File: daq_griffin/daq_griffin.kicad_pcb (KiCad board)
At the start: 4 copper layers, 80 x 117 mm, 203 parts, among them J1 SENSOR, J10 SENSOR, J11 SENSOR, J12 SENSOR, J13 SENSOR, J14 SENSOR, J15 SENSOR, J16 SENSOR, J17 SENSOR, J18 SENSOR, J19 SENSOR, J2 SENSOR, J20 SENSOR, J21 SENSOR, J22 SENSOR, J23 SENSOR, J24 SENSOR, J25 POWER_12V, J26 I2C Header, J27 CAN Header, J3 SENSOR, J4 SENSOR, J5 SENSOR, J6 SENSOR, J7 SENSOR, J8 SENSOR, J9 SENSOR, U13 ADS8866, U14 ADS8866, U15 ADS8866, U16 ADS8866, U17 ADS8866, U18 ADS8866, U19 ADS8866, U20 ADS8866, U21 ADS8866, U22 ADS8866, U23 ADS8866, U24 ADS8866, U25 TPS54302, U26 Teensy4.1, U29 REF6050xDGK, U30 TLV70933, U55 TCAN3414

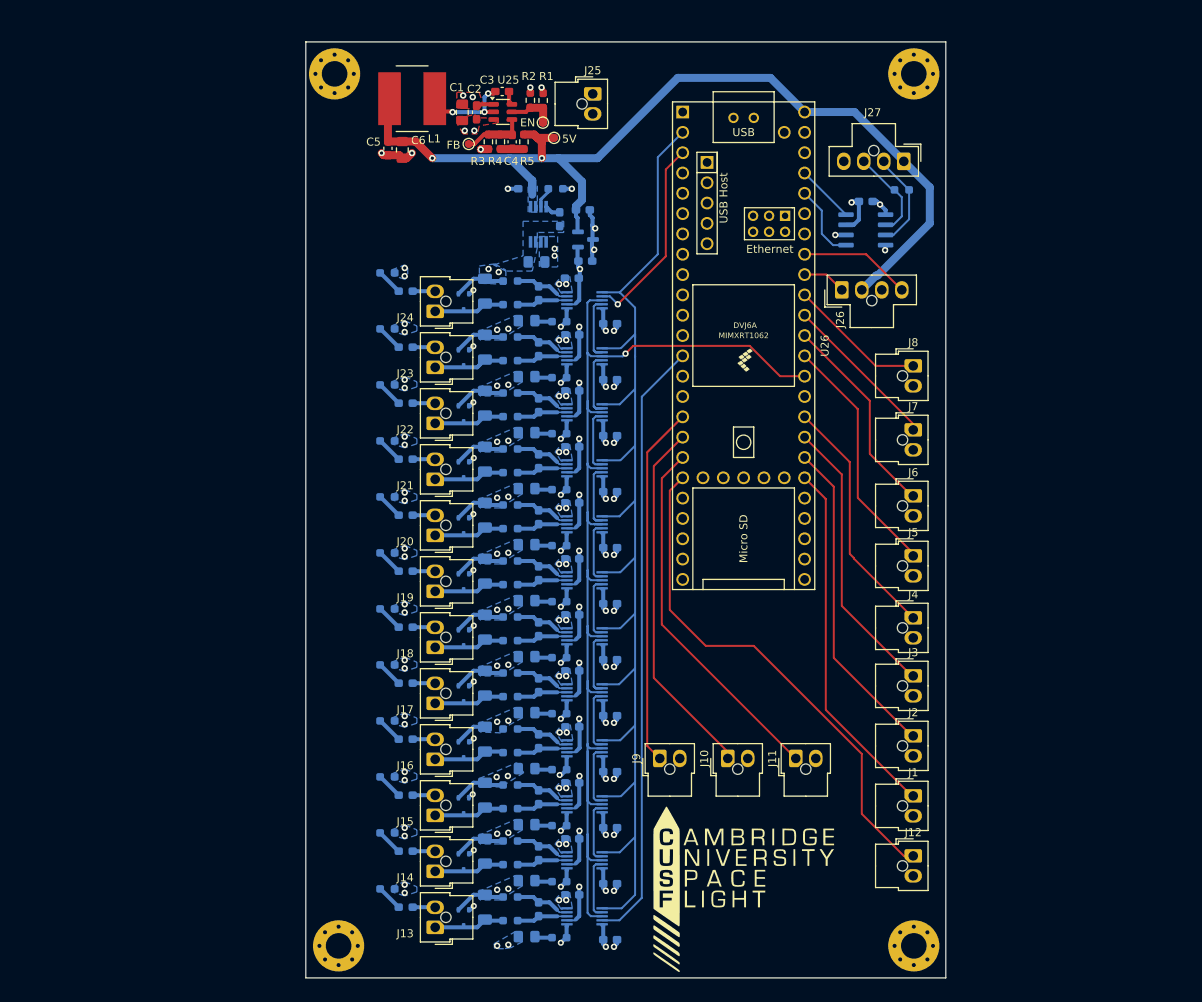
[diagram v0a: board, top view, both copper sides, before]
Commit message: Add 24V capability, add feed systems motor connections, fix SPI connections, add ignitor board connections, add i2c connections.
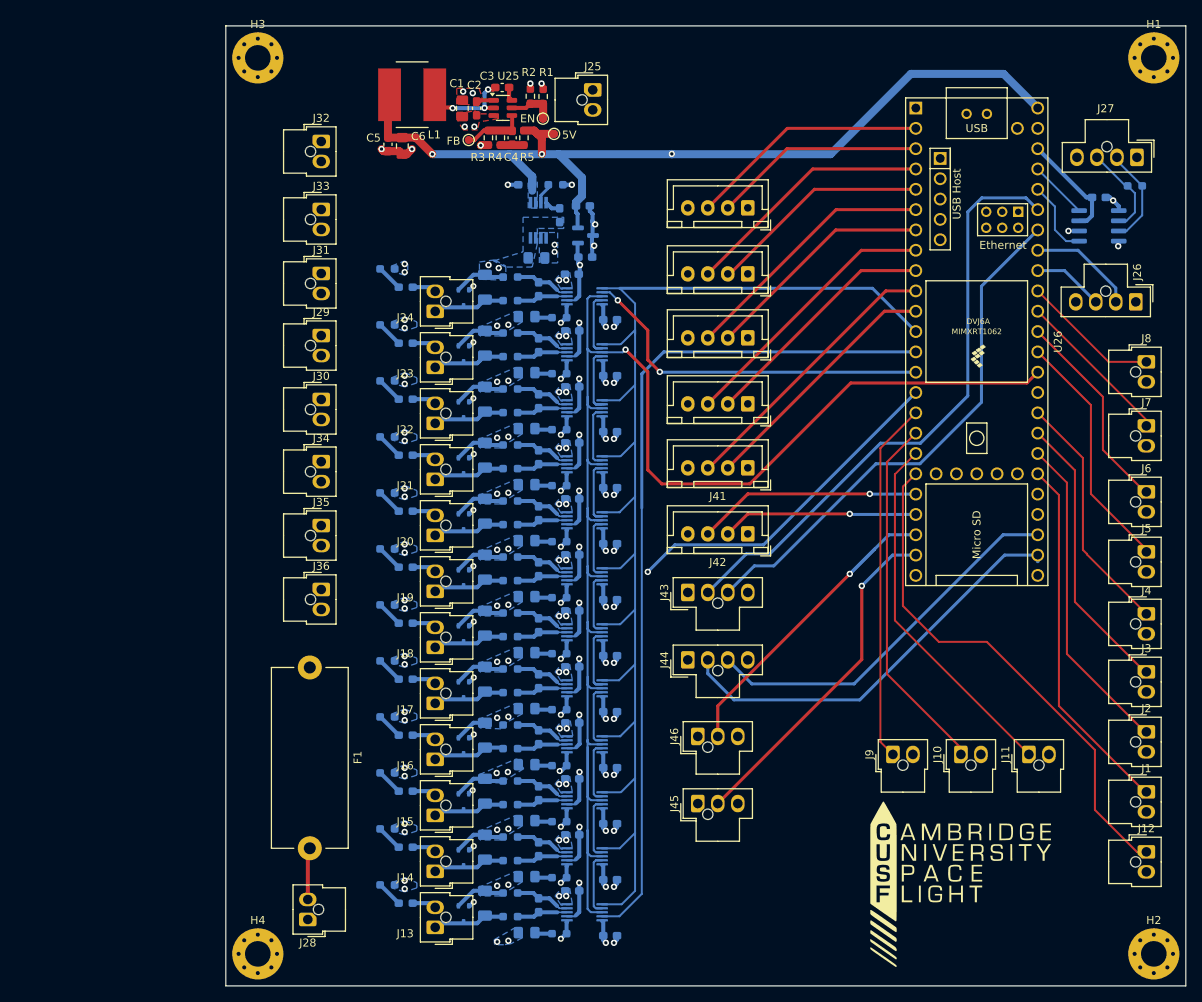
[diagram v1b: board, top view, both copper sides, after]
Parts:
- removed REF**, REF**1, REF**2, REF**3: MountingHole_3.2mm_M3_Pad_Via, MountingHole:MountingHole_3.2mm_M3_Pad_Via
- added F1: Fuse, Fuse:Fuseholder_Cylinder-5x20mm_Stelvio-Kontek_PTF78_Horizontal_Open, F.Cu at (90.5, 138.2)
- added H1: MountingHole_Pad, MountingHole:MountingHole_3.2mm_M3_Pad_Via, F.Cu at (196.0, 62.0)
- added H2: MountingHole_Pad, MountingHole:MountingHole_3.2mm_M3_Pad_Via, F.Cu at (196.0, 174.0)
- added H3: MountingHole_Pad, MountingHole:MountingHole_3.2mm_M3_Pad_Via, F.Cu at (84.0, 62.0)
- added H4: MountingHole_Pad, MountingHole:MountingHole_3.2mm_M3_Pad_Via, F.Cu at (84.0, 174.0)
- added J28: POWER_24V, Connector_Molex:Molex_Nano-Fit_105309-xx02_1x02_P2.50mm_Vertical, F.Cu at (90.2, 169.7)
- added J29: POWER_12V, Connector_Molex:Molex_Nano-Fit_105309-xx02_1x02_P2.50mm_Vertical, F.Cu at (91.9, 96.7)
- added J30: POWER_12V, Connector_Molex:Molex_Nano-Fit_105309-xx02_1x02_P2.50mm_Vertical, F.Cu at (91.9, 104.7)
- added J31: POWER_12V, Connector_Molex:Molex_Nano-Fit_105309-xx02_1x02_P2.50mm_Vertical, F.Cu at (91.9, 89.0)
- added J32: POWER_12V, Connector_Molex:Molex_Nano-Fit_105309-xx02_1x02_P2.50mm_Vertical, F.Cu at (91.9, 72.5)
- added J33: POWER_12V, Connector_Molex:Molex_Nano-Fit_105309-xx02_1x02_P2.50mm_Vertical, F.Cu at (91.9, 81.0)
- added J34: POWER_12V, Connector_Molex:Molex_Nano-Fit_105309-xx02_1x02_P2.50mm_Vertical, F.Cu at (91.9, 112.5)
- added J35: POWER_12V, Connector_Molex:Molex_Nano-Fit_105309-xx02_1x02_P2.50mm_Vertical, F.Cu at (91.9, 120.5)
- added J36: POWER_12V, Connector_Molex:Molex_Nano-Fit_105309-xx02_1x02_P2.50mm_Vertical, F.Cu at (91.9, 128.4)
- added J37: Conn_01x04_Socket, Connector_JST:JST_XH_B4B-XH-A_1x04_P2.50mm_Vertical, F.Cu at (145.2, 89.0)
- added J38: Conn_01x04_Socket, Connector_JST:JST_XH_B4B-XH-A_1x04_P2.50mm_Vertical, F.Cu at (145.2, 80.8)
- added J39: Conn_01x04_Socket, Connector_JST:JST_XH_B4B-XH-A_1x04_P2.50mm_Vertical, F.Cu at (145.2, 97.0)
- added J40: Conn_01x04_Socket, Connector_JST:JST_XH_B4B-XH-A_1x04_P2.50mm_Vertical, F.Cu at (145.2, 105.2)
- added J41: Conn_01x04_Socket, Connector_JST:JST_XH_B4B-XH-A_1x04_P2.50mm_Vertical, F.Cu at (145.2, 113.2)
- added J42: Conn_01x04_Socket, Connector_JST:JST_XH_B4B-XH-A_1x04_P2.50mm_Vertical, F.Cu at (145.2, 121.5)
- added J43: UART Header, Connector_Molex:Molex_Nano-Fit_105309-xx04_1x04_P2.50mm_Vertical, F.Cu at (137.8, 128.8)
- added J44: UART Header, Connector_Molex:Molex_Nano-Fit_105309-xx04_1x04_P2.50mm_Vertical, F.Cu at (137.8, 137.2)
- added J45: Conn_01x03_Socket, Connector_Molex:Molex_Nano-Fit_105309-xx03_1x03_P2.50mm_Vertical, F.Cu at (139.0, 155.2)
- added J46: Conn_01x03_Socket, Connector_Molex:Molex_Nano-Fit_105309-xx03_1x03_P2.50mm_Vertical, F.Cu at (139.0, 146.8)
- moved J26 36.8 mm to (193.8, 92.5), turned to -90 degrees
- moved U26 29.1 mm to (173.9, 97.5)
- moved C113 29.1 mm to (189.1, 79.4)
- moved J1 29.1 mm to (195.1, 153.8)
- moved J10 29.1 mm to (171.9, 149.1)
- moved J11 29.1 mm to (180.4, 149.1)
- moved J12 29.1 mm to (195.1, 161.2)
- moved J2 29.1 mm to (195.1, 146.2)
- moved J27 29.1 mm to (193.9, 74.4)
- moved J3 29.1 mm to (195.1, 138.8)
- moved J4 29.1 mm to (195.1, 131.5)
- moved J5 29.1 mm to (195.1, 123.8)
- moved J6 29.1 mm to (195.1, 116.2)
- moved J7 29.1 mm to (195.1, 108.0)
- moved J8 29.1 mm to (195.1, 100.0)
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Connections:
- net /MOSI2 renamed /ADC_Chain2/MOSI
- C113 pad 1: +3.3V -> Net-(U55-VCC)
- J11 pad 1: Net-(J11-Pin_1) -> GND
- J26 pad 1: Net-(J26-Pin_1) -> GND
- J26 pad 2: +5V -> Net-(J26-Pin_2)
- J26 pad 3: GND -> Net-(J26-Pin_3)
- J26 pad 4: Net-(J26-Pin_4) -> +5V
- J27 pad 1: +5V -> GND
- J27 pad 4: GND -> +5V
- U26 pad 10: unconnected-(U26-8_TX2_IN1-Pad10) -> Net-(J41-Pin_3)
- U26 pad 11: unconnected-(U26-9_OUT1C-Pad11) -> Net-(J41-Pin_2)
- U26 pad 12: unconnected-(U26-10_CS_MQSR-Pad12) -> /ADC_Chain2/CS
- U26 pad 14: unconnected-(U26-12_MISO_MQSL-Pad14) -> /ADC_Chain2/MISO
- U26 pad 15: unconnected-(U26-3V3-Pad15) -> +3.3V
- U26 pad 18: Net-(J11-Pin_1) -> GND
- U26 pad 2: /ADC_Chain2/CS -> Net-(J38-Pin_3)
- U26 pad 20: unconnected-(U26-28_RX7-Pad20) -> Net-(J42-Pin_3)
- U26 pad 21: unconnected-(U26-29_TX7-Pad21) -> Net-(J42-Pin_2)
- U26 pad 22: unconnected-(U26-30_CRX3-Pad22) -> Net-(J46-Pin_2)
- U26 pad 23: unconnected-(U26-31_CTX3-Pad23) -> Net-(J45-Pin_2)
- U26 pad 26: unconnected-(U26-34_RX8-Pad26) -> Net-(J44-Pin_2)
- U26 pad 27: unconnected-(U26-35_TX8-Pad27) -> Net-(J44-Pin_3)
- U26 pad 3: /ADC_Chain2/MISO -> Net-(J38-Pin_2)
- U26 pad 4: unconnected-(U26-2_OUT2-Pad4) -> Net-(J37-Pin_3)
- U26 pad 40: Net-(J26-Pin_1) -> Net-(J26-Pin_3)
- U26 pad 41: Net-(J26-Pin_4) -> Net-(J26-Pin_2)
- U26 pad 42: unconnected-(U26-20_A6_TX5_LRCLK1-Pad42) -> Net-(J43-Pin_3)
- U26 pad 43: unconnected-(U26-21_A7_RX5_BCLK1-Pad43) -> Net-(J43-Pin_2)
- U26 pad 46: +3.3V -> Net-(U55-VCC)
- U26 pad 5: unconnected-(U26-3_LRCLK2-Pad5) -> Net-(J37-Pin_2)
- U26 pad 6: unconnected-(U26-4_BCLK2-Pad6) -> Net-(J39-Pin_3)
- U26 pad 7: unconnected-(U26-5_IN2-Pad7) -> Net-(J39-Pin_2)
- U26 pad 8: unconnected-(U26-6_OUT1D-Pad8) -> Net-(J40-Pin_3)
- U26 pad 9: unconnected-(U26-7_RX2_OUT1A-Pad9) -> Net-(J40-Pin_2)
- U55 pad 3: +3.3V -> Net-(U55-VCC)
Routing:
- net Net-(J43-Pin_2): track 0.00 -> 75.8 mm
- net Net-(J43-Pin_3): track 0.00 -> 66.0 mm
- net Net-(J44-Pin_2): track 0.00 -> 52.6 mm
- net Net-(J44-Pin_3): track 0.00 -> 47.7 mm
- net /SCLK2: track 142.7 -> 189.8 mm
- net GND: track 108.4 -> 154.1 mm
- net Net-(J11-Pin_1): track 45.6 -> 0.00 mm
- net Net-(J45-Pin_2): track 0.00 -> 43.0 mm, vias 0 -> 1
- net Net-(J46-Pin_2): track 0.00 -> 41.8 mm, vias 0 -> 1
- net +3.3V: track 40.7 -> 78.3 mm
- net Net-(J41-Pin_3): track 0.00 -> 35.2 mm
- net Net-(J40-Pin_3): track 0.00 -> 34.0 mm
- net Net-(J39-Pin_3): track 0.00 -> 32.6 mm
- net Net-(J41-Pin_2): track 0.00 -> 31.6 mm
- net Net-(J37-Pin_3): track 0.00 -> 31.4 mm
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- added copper zone on In1.Cu, net +24V
- added copper zone on In1.Cu, net +5V
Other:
- board size 80 x 117 mm -> 120 x 120 mm

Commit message: Rewired right side and fixed dual transistor
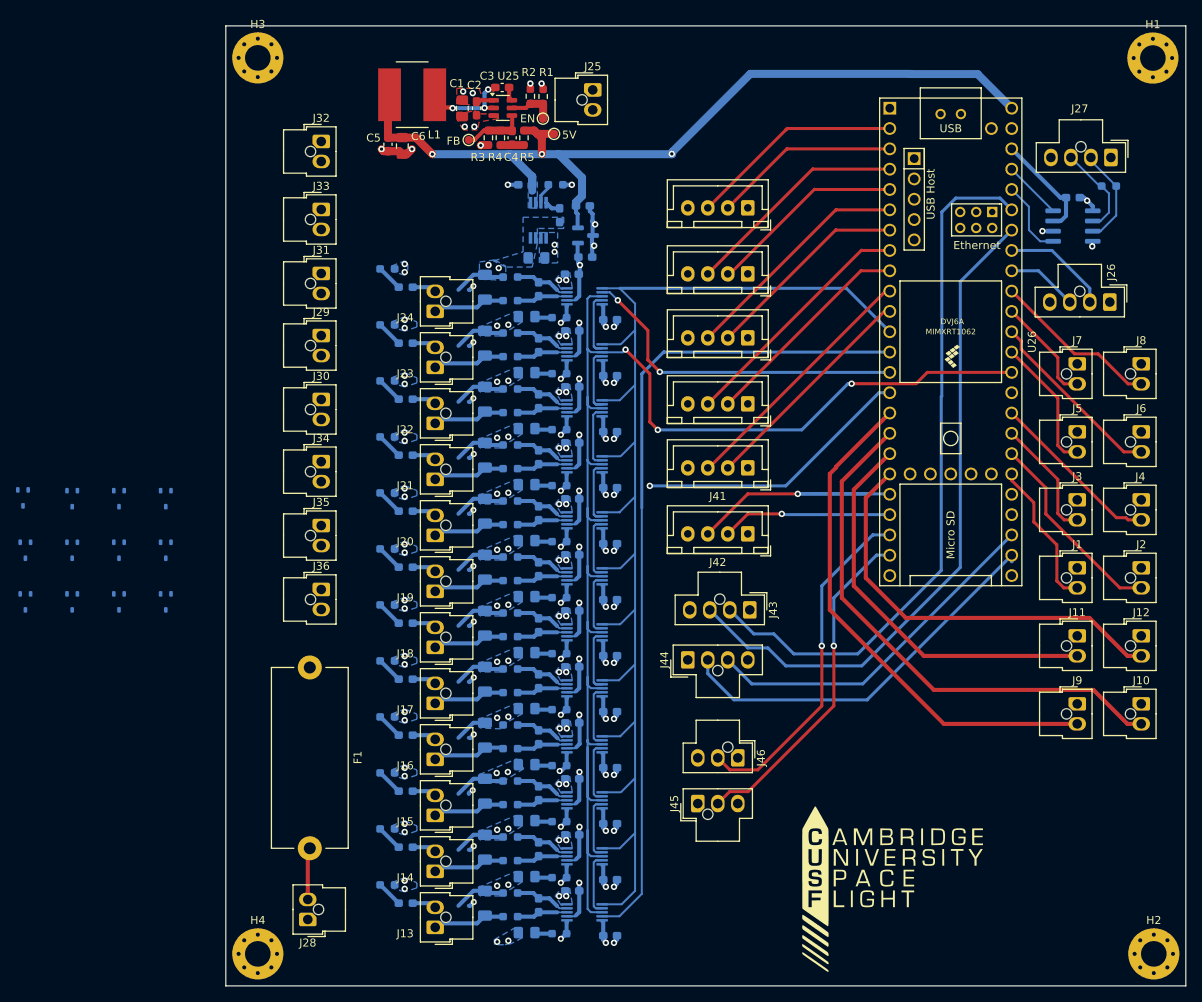
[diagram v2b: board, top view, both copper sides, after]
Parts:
- removed D13, D14, D15, D16, D17, D18, D19, D20, D21, D22, D23, D24: BAT54SW, Package_TO_SOT_SMD:SOT-323_SC-70
- added D1: BAV99, Package_TO_SOT_SMD:SOT-323_SC-70, B.Cu at (54.6, 117.0)
- added D10: BAV99, Package_TO_SOT_SMD:SOT-323_SC-70, B.Cu at (72.5, 130.0)
- added D11: BAV99, Package_TO_SOT_SMD:SOT-323_SC-70, B.Cu at (72.5, 117.1)
- added D12: BAV99, Package_TO_SOT_SMD:SOT-323_SC-70, B.Cu at (66.7, 117.1)
- added D2: BAV99, Package_TO_SOT_SMD:SOT-323_SC-70, B.Cu at (55.0, 130.0)
- added D3: BAV99, Package_TO_SOT_SMD:SOT-323_SC-70, B.Cu at (60.8, 130.0)
- added D4: BAV99, Package_TO_SOT_SMD:SOT-323_SC-70, B.Cu at (55.0, 123.5)
- added D5: BAV99, Package_TO_SOT_SMD:SOT-323_SC-70, B.Cu at (66.7, 123.5)
- added D6: BAV99, Package_TO_SOT_SMD:SOT-323_SC-70, B.Cu at (60.8, 117.1)
- added D7: BAV99, Package_TO_SOT_SMD:SOT-323_SC-70, B.Cu at (60.8, 123.5)
- added D8: BAV99, Package_TO_SOT_SMD:SOT-323_SC-70, B.Cu at (66.7, 130.0)
- added D9: BAV99, Package_TO_SOT_SMD:SOT-323_SC-70, B.Cu at (72.5, 123.5)
- J29, J30, J31, J32, J33, J34, J35, J36: value POWER_12V -> POWER_24V
- moved J1 29.3 mm to (186.4, 125.8)
- moved J12 27.0 mm to (194.4, 134.2)
- moved J9 23.9 mm to (186.4, 142.8), turned to 0 degrees
- moved J10 23.4 mm to (194.4, 142.8), turned to 0 degrees
- moved J3 23.2 mm to (186.4, 117.2)
- moved J2 20.5 mm to (194.4, 125.8)
- moved J5 17.3 mm to (186.4, 108.8)
- moved J11 16.0 mm to (186.4, 134.2), turned to 0 degrees
- moved J4 14.3 mm to (194.4, 117.2)
- moved J7 11.6 mm to (186.4, 100.2)
- moved J43 8.05 mm to (145.5, 131.0), turned to -90 degrees
- moved J6 7.53 mm to (194.4, 108.8)
- moved J46 5.67 mm to (144.0, 149.5), turned to -90 degrees
- moved C113 3.25 mm to (185.9, 79.5)
- moved J26 3.25 mm to (190.5, 92.5)
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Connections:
- J1 pad 1: Net-(J1-Pin_1) -> GND
- J1 pad 2: GND -> Net-(J1-Pin_2)
- J10 pad 1: Net-(J10-Pin_1) -> GND
- J10 pad 2: GND -> Net-(J10-Pin_2)
- J11 pad 2: GND -> Net-(J11-Pin_2)
- J12 pad 1: Net-(J12-Pin_1) -> GND
- J12 pad 2: GND -> Net-(J12-Pin_2)
- J2 pad 1: Net-(J2-Pin_1) -> GND
- J2 pad 2: GND -> Net-(J2-Pin_2)
- J3 pad 1: Net-(J3-Pin_1) -> GND
- J3 pad 2: GND -> Net-(J3-Pin_2)
- J4 pad 1: Net-(J4-Pin_1) -> GND
- J4 pad 2: GND -> Net-(J4-Pin_2)
- J45 pad 1: +5V -> GND
- J45 pad 3: GND -> +5V
- J46 pad 1: +5V -> GND
- J46 pad 3: GND -> +5V
- J5 pad 1: Net-(J5-Pin_1) -> GND
- J5 pad 2: GND -> Net-(J5-Pin_2)
- J6 pad 1: Net-(J6-Pin_1) -> GND
- J6 pad 2: GND -> Net-(J6-Pin_2)
- J7 pad 1: Net-(J7-Pin_1) -> GND
- J7 pad 2: GND -> Net-(J7-Pin_2)
- J8 pad 1: Net-(J8-Pin_1) -> GND
- J8 pad 2: GND -> Net-(J8-Pin_2)
- J9 pad 1: Net-(J9-Pin_1) -> GND
- J9 pad 2: GND -> Net-(J9-Pin_2)
- U26 pad 16: Net-(J9-Pin_1) -> Net-(J9-Pin_2)
- U26 pad 17: Net-(J10-Pin_1) -> Net-(J10-Pin_2)
- U26 pad 18: GND -> Net-(J11-Pin_2)
- U26 pad 19: Net-(J12-Pin_1) -> Net-(J12-Pin_2)
- U26 pad 30: Net-(J1-Pin_1) -> Net-(J1-Pin_2)
- U26 pad 31: Net-(J2-Pin_1) -> Net-(J2-Pin_2)
- U26 pad 32: Net-(J3-Pin_1) -> Net-(J3-Pin_2)
- U26 pad 33: Net-(J4-Pin_1) -> Net-(J4-Pin_2)
- U26 pad 36: Net-(J5-Pin_1) -> Net-(J5-Pin_2)
- U26 pad 37: Net-(J6-Pin_1) -> Net-(J6-Pin_2)
- U26 pad 38: Net-(J7-Pin_1) -> Net-(J7-Pin_2)
- U26 pad 39: Net-(J8-Pin_1) -> Net-(J8-Pin_2)
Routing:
- net Net-(J10-Pin_2): track 0.00 -> 67.0 mm
- net Net-(J12-Pin_1): track 64.7 -> 0.00 mm
- net Net-(J9-Pin_2): track 0.00 -> 64.5 mm
- net Net-(J12-Pin_2): track 0.00 -> 52.7 mm
- net Net-(J11-Pin_2): track 0.00 -> 49.9 mm
- net GND: track 154.1 -> 108.4 mm
- net Net-(J1-Pin_1): track 45.5 -> 0.00 mm
- net Net-(J10-Pin_1): track 45.5 -> 0.00 mm
- net Net-(J9-Pin_1): track 45.2 -> 0.00 mm
- net Net-(J2-Pin_1): track 40.5 -> 0.00 mm
- net Net-(J3-Pin_1): track 35.6 -> 0.00 mm
- net Net-(J4-Pin_1): track 30.8 -> 0.00 mm
- net Net-(J5-Pin_1): track 30.6 -> 0.00 mm
- net Net-(J6-Pin_1): track 25.8 -> 0.00 mm
- net Net-(J2-Pin_2): track 0.00 -> 25.1 mm
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
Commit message: Complete Silkscreen
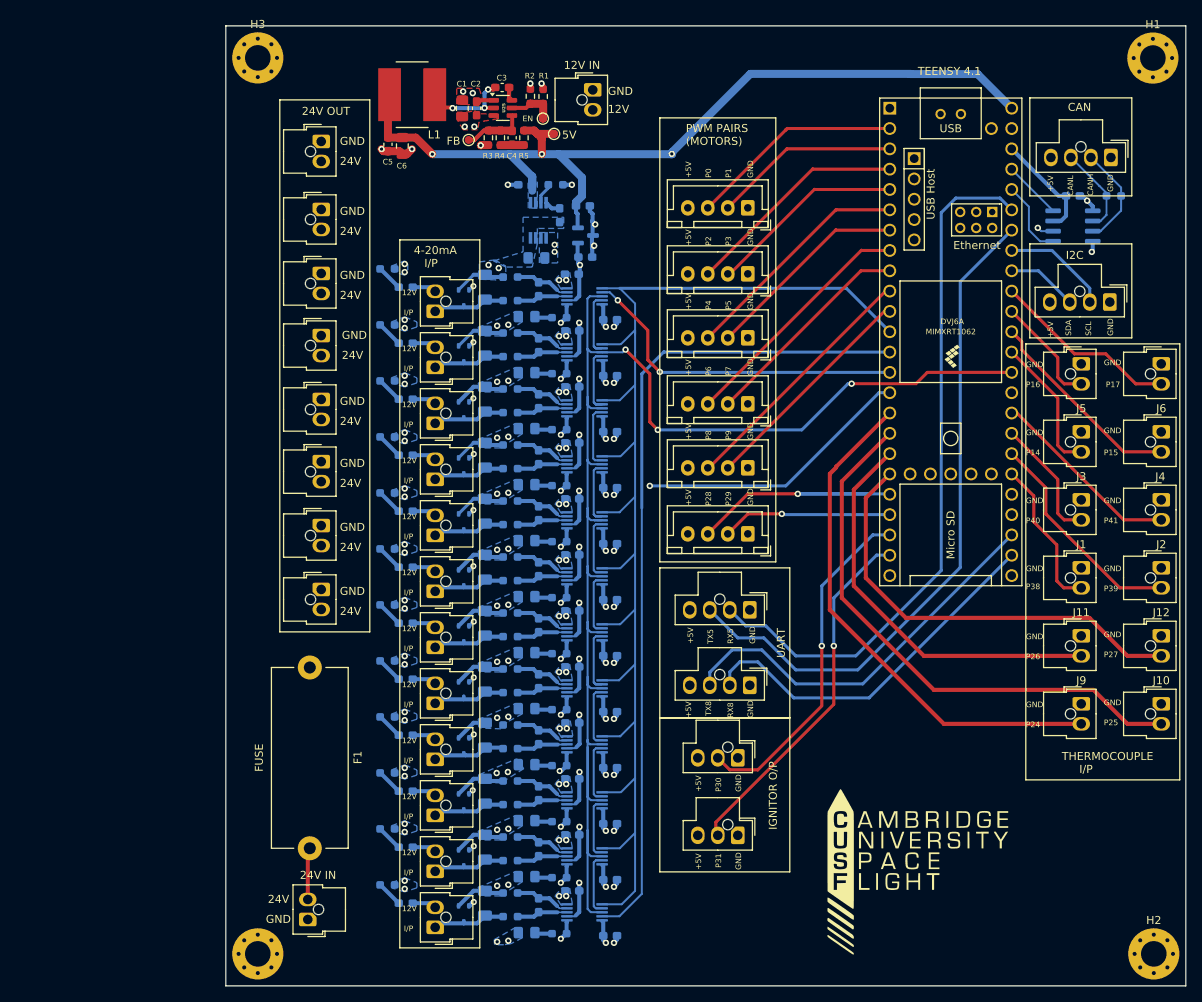
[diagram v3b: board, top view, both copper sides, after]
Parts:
- moved D1 71.1 mm to (109.8, 162.0)
- moved D3 62.6 mm to (109.8, 169.0)
- moved D2 60.2 mm to (109.8, 155.0)
- moved D4 57.5 mm to (109.8, 141.0)
- moved D6 49.9 mm to (109.8, 127.0)
- moved D12 49.9 mm to (109.8, 92.0)
- moved D7 49.1 mm to (109.8, 120.0)
- moved D10 48.5 mm to (109.8, 99.0)
- moved D11 48.4 mm to (109.8, 148.0)
- moved D8 46.3 mm to (109.8, 113.0)
- moved D5 44.3 mm to (109.8, 134.0)
- moved D9 41.2 mm to (109.8, 106.0)
- moved J44 8.38 mm to (145.5, 140.4), turned to -90 degrees
- moved J45 6.38 mm to (144.0, 159.2), turned to -90 degrees
- moved J10 2.50 mm to (196.9, 142.8)
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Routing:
- net Net-(J44-Pin_3): track 44.4 -> 50.0 mm
- net Net-(J45-Pin_2): track 42.6 -> 45.4 mm
- net Net-(J44-Pin_2): track 49.3 -> 46.7 mm
- net Net-(J2-Pin_2): track 25.1 -> 27.6 mm
- net Net-(J8-Pin_2): track 21.0 -> 23.5 mm
- net Net-(J6-Pin_2): track 23.0 -> 25.5 mm
- net Net-(J12-Pin_2): track 52.7 -> 55.2 mm
- net Net-(J10-Pin_2): track 67.0 -> 69.5 mm
- net Net-(J4-Pin_2): track 21.7 -> 24.2 mm
- net GND: track 108.4 -> 110.0 mm
- net Net-(J27-Pin_2): track 12.3 -> 13.2 mm
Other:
- board text added: "+5V"
- board text added: "12V"
- board text added: "12V IN"
- board text added: "24V"
- board text added: "24V IN"
- board text added: "24V OUT"
- board text added: "4-20mA I/P"
- board text added: "CAN"
- board text added: "CANH"
- board text added: "CANL"
- board text added: "FUSE"
- board text added: "GND"
- board text added: "I/P"
- board text added: "I2C"
- board text added: "IGNITOR O/P"
- board text added: "P0"
- board text added: "P1"
- board text added: "P14"
- board text added: "P15"
- board text added: "P16"
- board text added: "P17"
- board text added: "P2"
- board text added: "P24"
- board text added: "P25"
- board text added: "P26"
- board text added: "P27"
- board text added: "P28"
- board text added: "P29"
- board text added: "P3"
- board text added: "P30"
- board text added: "P31"
- board text added: "P38"
- board text added: "P39"
- board text added: "P4"
- board text added: "P40"
- board text added: "P41"
- board text added: "P5"
- board text added: "P6"
- board text added: "P7"
- board text added: "P8"
- board text added: "P9"
- board text added: "PWM PAIRS (MOTORS)"
- board text added: "RX5"
- board text added: "RX8"
- board text added: "SCL"
- board text added: "SDA"
- board text added: "TEENSY 4.1"
- board text added: "THERMOCOUPLE I/P"
- board text added: "TX5"
- board text added: "TX8"
- board text added: "UART"
